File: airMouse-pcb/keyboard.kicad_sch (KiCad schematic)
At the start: 69 parts, among them SW1 TACT, SW10 TACT, SW11 TACT, SW12 TACT, SW13 TACT, SW14 TACT, SW15 TACT, SW16 TACT, SW17 TACT, SW18 TACT, SW19 TACT, SW2 TACT, SW20 TACT, SW21 TACT, SW22 TACT, SW23 TACT, SW24 TACT, SW25 TACT, SW26 TACT, SW27 TACT, SW28 TACT, SW29 TACT, SW3 TACT, SW30 TACT, SW31 TACT, SW32 TACT, SW33 TACT, SW34 TACT, SW35 TACT, SW36 TACT, SW37 TACT, SW38 TACT, SW39 TACT, SW4 TACT, SW40 TACT, SW41 TACT, SW42 TACT, SW43 TACT, SW44 TACT, SW45 TACT, SW46 TACT, SW47 TACT, SW48 TACT, SW49 TACT, SW5 TACT, SW6 TACT, SW7 TACT, SW8 TACT, SW9 TACT

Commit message: key footprint
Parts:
- SW1, SW10, SW11, SW12, SW13, SW14, SW15, SW16, SW17, SW18, SW19, SW2, SW20, SW21, SW22, SW23, SW24, SW25, SW26, SW27, SW28, SW29, SW3, SW30, SW31, SW32, SW33, SW34, SW35, SW36, SW37, SW38, SW39, SW4, SW40, SW41, SW42, SW43, SW44, SW45, SW46, SW47, SW48, SW49, SW5, SW6, SW7, SW8, SW9: footprint (none) -> airMouseLib:TL3315NF100Q
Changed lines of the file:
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@@
 			)
 		)
-		(property "Footprint" ""
+		(property "Footprint" "airMouseLib:TL3315NF100Q"
 			(at 68.58 100.33 0)
 			(effects
@@
 			)
 		)
-		(property "Footprint" ""
+		(property "Footprint" "airMouseLib:TL3315NF100Q"
 			(at 132.08 115.57 0)
 			(effects
@@
 			)
 		)
-		(property "Footprint" ""
+		(property "Footprint" "airMouseLib:TL3315NF100Q"
 			(at 106.68 100.33 0)
 			(effects
@@
 			)
 		)
-		(property "Footprint" ""
+		(property "Footprint" "airMouseLib:TL3315NF100Q"
 			(at 132.08 100.33 0)
 			(effects
@@
 			)
 		)
-		(property "Footprint" ""
+		(property "Footprint" "airMouseLib:TL3315NF100Q"
 			(at 170.18 85.09 0)
 			(effects
@@
 			)
 		)
-		(property "Footprint" ""
+		(property "Footprint" "airMouseLib:TL3315NF100Q"
 			(at 170.18 69.85 0)
 			(effects
@@
 			)
 		)
-		(property "Footprint" ""
+		(property "Footprint" "airMouseLib:TL3315NF100Q"
 			(at 144.78 100.33 0)
 			(effects
@@
 			)
 		)
-		(property "Footprint" ""
+		(property "Footprint" "airMouseLib:TL3315NF100Q"
 			(at 157.48 115.57 0)
 			(effects
@@
 			)
 		)
-		(property "Footprint" ""
+		(property "Footprint" "airMouseLib:TL3315NF100Q"
 			(at 182.88 130.81 0)
 			(effects
@@
 			)
 		)
-		(property "Footprint" ""
+		(property "Footprint" "airMouseLib:TL3315NF100Q"
 			(at 144.78 85.09 0)
 			(effects
@@
 			)
 		)
-		(property "Footprint" ""
+		(property "Footprint" "airMouseLib:TL3315NF100Q"
 			(at 157.48 85.09 0)
 			(effects
@@
 			)
 		)
-		(property "Footprint" ""
+		(property "Footprint" "airMouseLib:TL3315NF100Q"
 			(at 93.98 100.33 0)
 			(effects
@@
 			)
 		)
-		(property "Footprint" ""
+		(property "Footprint" "airMouseLib:TL3315NF100Q"
 			(at 125.73 130.81 0)
 			(effects
@@
 			)
 		)
-		(property "Footprint" ""
+		(property "Footprint" "airMouseLib:TL3315NF100Q"
 			(at 170.18 130.81 0)
 			(effects
@@
 			)
 		)
-		(property "Footprint" ""
+		(property "Footprint" "airMouseLib:TL3315NF100Q"
 			(at 170.18 115.57 0)
 			(effects
@@
 			)
 		)
-		(property "Footprint" ""
+		(property "Footprint" "airMouseLib:TL3315NF100Q"
 			(at 170.18 100.33 0)
 			(effects
@@
 			)
 		)
-		(property "Footprint" ""
+		(property "Footprint" "airMouseLib:TL3315NF100Q"
 			(at 119.38 85.09 0)
 			(effects
@@
 			)
 		)
-		(property "Footprint" ""
+		(property "Footprint" "airMouseLib:TL3315NF100Q"
 			(at 182.88 115.57 0)
 			(effects
@@
 			)
 		)
-		(property "Footprint" ""
+		(property "Footprint" "airMouseLib:TL3315NF100Q"
 			(at 68.58 115.57 0)
 			(effects
@@
 			)
 		)
-		(property "Footprint" ""
+		(property "Footprint" "airMouseLib:TL3315NF100Q"
 			(at 119.38 115.57 0)
 			(effects
@@
 			)
 		)
-		(property "Footprint" ""
+		(property "Footprint" "airMouseLib:TL3315NF100Q"
 			(at 81.28 69.85 0)
 			(effects
@@
 			)
 		)
-		(property "Footprint" ""
+		(property "Footprint" "airMouseLib:TL3315NF100Q"
 			(at 81.28 100.33 0)
 			(effects
@@
 			)
 		)
-		(property "Footprint" ""
+		(property "Footprint" "airMouseLib:TL3315NF100Q"
 			(at 182.88 85.09 0)
 			(effects
@@
 			)
 		)
-		(property "Footprint" ""
+		(property "Footprint" "airMouseLib:TL3315NF100Q"
 			(at 81.28 115.57 0)
 			(effects
@@
 			)
 		)
-		(property "Footprint" ""
+		(property "Footprint" "airMouseLib:TL3315NF100Q"
 			(at 144.78 115.57 0)
 			(effects
@@
 			)
 		)
-		(property "Footprint" ""
+		(property "Footprint" "airMouseLib:TL3315NF100Q"
 			(at 119.38 100.33 0)
 			(effects
@@
 			)
 		)
-		(property "Footprint" ""
+		(property "Footprint" "airMouseLib:TL3315NF100Q"
 			(at 182.88 69.85 0)
 			(effects
@@
 			)
 		)
-		(property "Footprint" ""
+		(property "Footprint" "airMouseLib:TL3315NF100Q"
 			(at 106.68 115.57 0)
 			(effects
@@
 			)
 		)
-		(property "Footprint" ""
+		(property "Footprint" "airMouseLib:TL3315NF100Q"
 			(at 119.38 69.85 0)
 			(effects
@@
 			)
 		)
-		(property "Footprint" ""
+		(property "Footprint" "airMouseLib:TL3315NF100Q"
 			(at 132.08 69.85 0)
 			(effects
@@
 			)
 		)
-		(property "Footprint" ""
+		(property "Footprint" "airMouseLib:TL3315NF100Q"
 			(at 157.48 100.33 0)
 			(effects
@@
 			)
 		)
-		(property "Footprint" ""
+		(property "Footprint" "airMouseLib:TL3315NF100Q"
 			(at 68.58 130.81 0)
 			(effects
@@
 			)
 		)
-		(property "Footprint" ""
+		(property "Footprint" "airMouseLib:TL3315NF100Q"
 			(at 81.28 130.81 0)
 			(effects
@@
 			)
 		)
-		(property "Footprint" ""
+		(property "Footprint" "airMouseLib:TL3315NF100Q"
 			(at 93.98 130.81 0)
 			(effects
@@
 			)
 		)
-		(property "Footprint" ""
+		(property "Footprint" "airMouseLib:TL3315NF100Q"
 			(at 93.98 85.09 0)
 			(effects
@@
 			)
 		)
-		(property "Footprint" ""
+		(property "Footprint" "airMouseLib:TL3315NF100Q"
 			(at 157.48 130.81 0)
 			(effects
@@
 			)
 		)
-		(property "Footprint" ""
+		(property "Footprint" "airMouseLib:TL3315NF100Q"
 			(at 81.28 85.09 0)
 			(effects
@@
 			)
 		)
-		(property "Footprint" ""
+		(property "Footprint" "airMouseLib:TL3315NF100Q"
 			(at 182.88 100.33 0)
 			(effects
@@
 			)
 		)
-		(property "Footprint" ""
+		(property "Footprint" "airMouseLib:TL3315NF100Q"
 			(at 144.78 69.85 0)
 			(effects
@@
 			)
 		)
-		(property "Footprint" ""
+		(property "Footprint" "airMouseLib:TL3315NF100Q"
 			(at 157.48 69.85 0)
 			(effects
@@
 			)
 		)
-		(property "Footprint" ""
+		(property "Footprint" "airMouseLib:TL3315NF100Q"
 			(at 93.98 69.85 0)
 			(effects
@@
 			)
 		)
-		(property "Footprint" ""
+		(property "Footprint" "airMouseLib:TL3315NF100Q"
 			(at 93.98 115.57 0)
 			(effects
@@
 			)
 		)
-		(property "Footprint" ""
+		(property "Footprint" "airMouseLib:TL3315NF100Q"
 			(at 68.58 69.85 0)
 			(effects
@@
 			)
 		)
-		(property "Footprint" ""
+		(property "Footprint" "airMouseLib:TL3315NF100Q"
 			(at 132.08 85.09 0)
 			(effects
@@
 			)
 		)
-		(property "Footprint" ""
+		(property "Footprint" "airMouseLib:TL3315NF100Q"
 			(at 106.68 130.81 0)
 			(effects
@@
 			)
 		)
-		(property "Footprint" ""
+		(property "Footprint" "airMouseLib:TL3315NF100Q"
 			(at 68.58 85.09 0)
 			(effects
@@
 			)
 		)
-		(property "Footprint" ""
+		(property "Footprint" "airMouseLib:TL3315NF100Q"
 			(at 144.78 130.81 0)
 			(effects
@@
 			)
 		)
-		(property "Footprint" ""
+		(property "Footprint" "airMouseLib:TL3315NF100Q"
 			(at 106.68 85.09 0)
 			(effects
@@
 			)
 		)
-		(property "Footprint" ""
+		(property "Footprint" "airMouseLib:TL3315NF100Q"
 			(at 106.68 69.85 0)
 			(effects

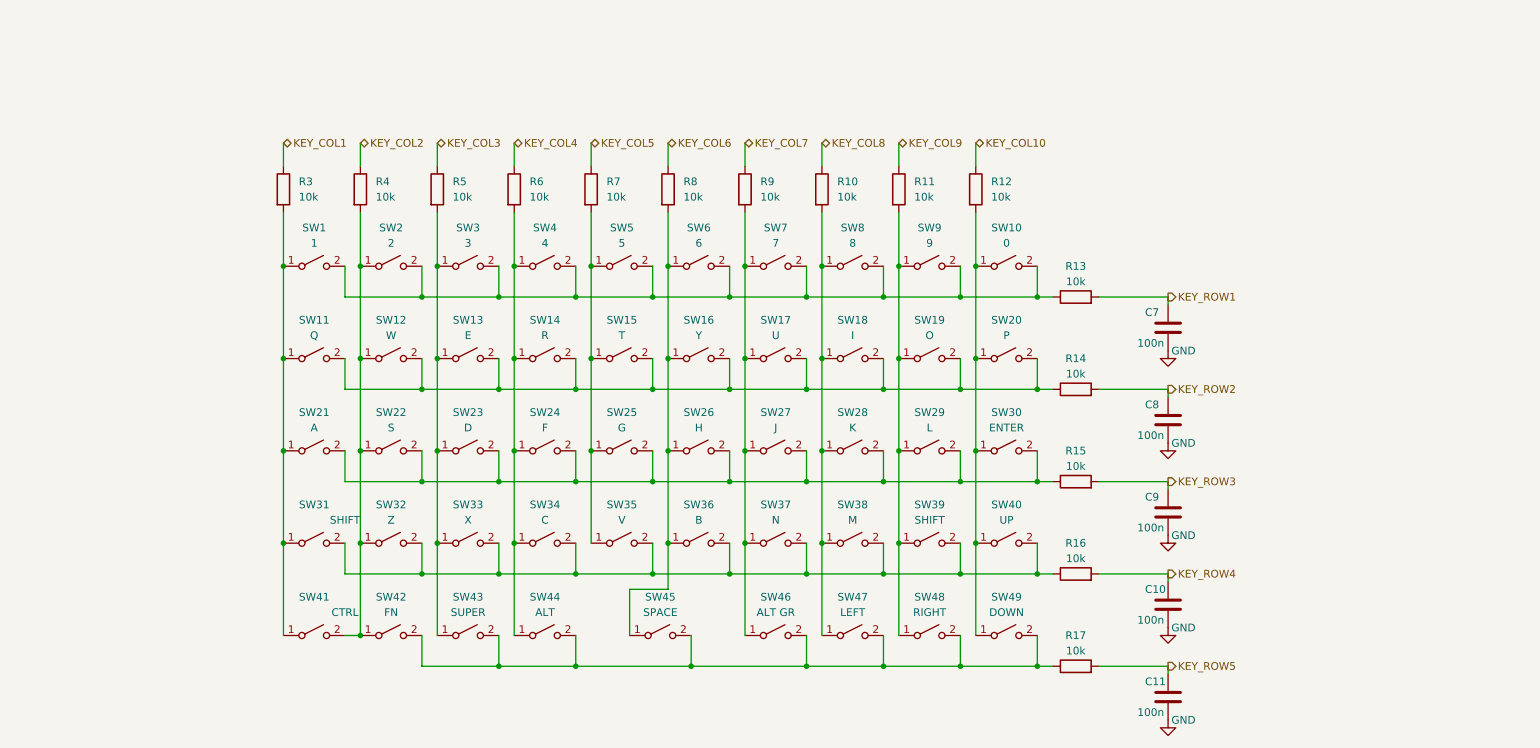
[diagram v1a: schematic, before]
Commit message: add keyboard
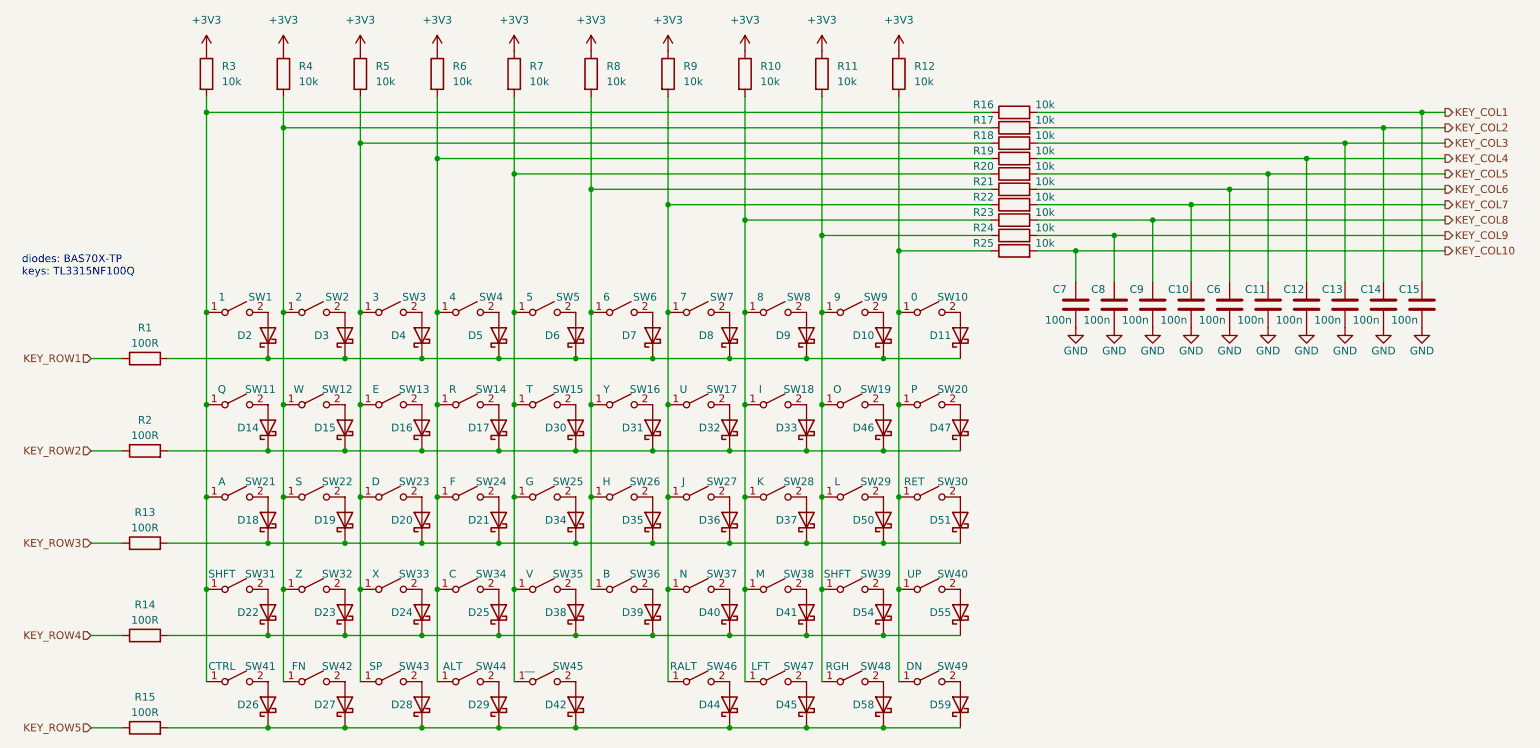
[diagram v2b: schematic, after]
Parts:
- removed SW1, SW10, SW11, SW12, SW13, SW14, SW15, SW16, SW17, SW18, SW19, SW2, SW20, SW21, SW22, SW23, SW24, SW25, SW26, SW27, SW28, SW29, SW3, SW30, SW31, SW32, SW33, SW34, SW35, SW36, SW37, SW38, SW39, SW4, SW40, SW41, SW42, SW43, SW44, SW45, SW46, SW47, SW48, SW49, SW5, SW6, SW7, SW8, SW9: TACT, airMouseLib:TL3315NF100Q, symbol Switch:SW_SPST
- added C12, C13, C14, C15, C6: 100n, Capacitor_SMD:C_0603_1608Metric, symbol Device:C
- added D10, D11, D14, D15, D16, D17, D18, D19, D2, D20, D21, D22, D23, D24, D25, D26, D27, D28, D29, D3, D30, D31, D32, D33, D34, D35, D36, D37, D38, D39, D4, D40, D41, D42, D44, D45, D46, D47, D5, D50, D51, D54, D55, D58, D59, D6, D7, D8, D9: BAS70X-TP, Diode_SMD:D_SOD-523, symbol Device:D_Schottky
- added R1, R2: 100R, Resistor_SMD:R_0603_1608Metric, symbol Device:R
- added R18, R19, R20, R21, R22, R23, R24, R25: 10k, Resistor_SMD:R_0603_1608Metric, symbol Device:R
- added SW1, SW10, SW11, SW12, SW13, SW14, SW15, SW16, SW17, SW18, SW19, SW2, SW20, SW21, SW22, SW23, SW24, SW25, SW26, SW27, SW28, SW29, SW3, SW30, SW31, SW32, SW33, SW34, SW35, SW36, SW37, SW38, SW39, SW4, SW40, SW41, SW42, SW43, SW44, SW45, SW46, SW47, SW48, SW49, SW5, SW6, SW7, SW8, SW9: KEY, airMouseLib:TL3315NF100Q, symbol airMouseLib:KEY
- C10, C11, C7, C8, C9: footprint (none) -> Capacitor_SMD:C_0603_1608Metric
- R10, R11, R12, R16, R17, R3, R4, R5, R6, R7, R8, R9: footprint (none) -> Resistor_SMD:R_0603_1608Metric
- R13, R14, R15: value 10k -> 100R; footprint (none) -> Resistor_SMD:R_0603_1608Metric
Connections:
- net GND: now also C12.2, C13.2, C14.2, C15.2, C6.2
- net KEY_COL1: now also R16.2, C15.1; no longer R3.1
- net KEY_COL10: now also C7.1, R25.2; no longer R12.1
- net KEY_COL2: now also R17.2, C14.1; no longer R4.1
- net KEY_COL3: now also C13.1, R18.2; no longer R5.1
- net KEY_COL4: now also C12.1, R19.2; no longer R6.1
- net KEY_COL5: now also C11.1, R20.2; no longer R7.1
- net KEY_COL6: now also C6.1, R21.2; no longer R8.1
- net KEY_COL7: now also C10.1, R22.2; no longer R9.1
- net KEY_COL8: now also C9.1, R23.2; no longer R10.1
- net KEY_COL9: now also C8.1, R24.2; no longer R11.1
- net KEY_ROW1: now also R1.1; no longer C7.1, R13.2
- net KEY_ROW2: now also R2.1; no longer C8.1, R14.2
- net KEY_ROW3: now also R13.1; no longer C9.1, R15.2
- net KEY_ROW4: now also R14.1; no longer C10.1, R16.2
- net KEY_ROW5: now also R15.1; no longer C11.1, R17.2
- net at R3.2: now also R16.1, SW1.1 (A), SW11.1 (A), SW21.1 (A), SW31.1 (A), SW41.1 (A)
- net at R6.2: now also R19.1, SW14.1 (A), SW24.1 (A), SW34.1 (A), SW4.1 (A), SW44.1 (A)
- net at R8.2: now also R21.1, SW16.1 (A), SW26.1 (A), SW36.1 (A), SW6.1 (A)
- net at R11.2: now also R24.1, SW19.1 (A), SW29.1 (A), SW39.1 (A), SW48.1 (A), SW9.1 (A)
- net at R9.2: now also R22.1, SW17.1 (A), SW27.1 (A), SW37.1 (A), SW46.1 (A), SW7.1 (A)
- net at R10.2: now also R23.1, SW18.1 (A), SW28.1 (A), SW38.1 (A), SW47.1 (A), SW8.1 (A)
- net at R12.2: now also R25.1, SW10.1 (A), SW20.1 (A), SW30.1 (A), SW40.1 (A), SW49.1 (A)
- net at R17.1: now also R4.2, SW12.1 (A), SW2.1 (A), SW22.1 (A), SW32.1 (A), SW42.1 (A)
- net at R5.2: now also R18.1, SW13.1 (A), SW23.1 (A), SW3.1 (A), SW33.1 (A), SW43.1 (A)
- net at R7.2: now also R20.1, SW15.1 (A), SW25.1 (A), SW35.1 (A), SW45.1 (A), SW5.1 (A)
- new net: D9.2 (A), SW8.2 (B)
- new net: D40.2 (A), SW37.2 (B)
- new net: D26.1 (K), D27.1 (K), D28.1 (K), D29.1 (K), D42.1 (K), D44.1 (K), D45.1 (K), D58.1 (K), D59.1 (K), R15.2
- new net: D26.2 (A), SW41.2 (B)
- new net: D32.2 (A), SW17.2 (B)
- new net: D10.1 (K), D11.1 (K), D2.1 (K), D3.1 (K), D4.1 (K), D5.1 (K), D6.1 (K), D7.1 (K), D8.1 (K), D9.1 (K), R1.2
- new net: D3.2 (A), SW2.2 (B)
- new net: D14.1 (K), D15.1 (K), D16.1 (K), D17.1 (K), D30.1 (K), D31.1 (K), D32.1 (K), D33.1 (K), D46.1 (K), D47.1 (K), R2.2
- new net: D30.2 (A), SW15.2 (B)
- new net: D42.2 (A), SW45.2 (B)
- new net: D18.1 (K), D19.1 (K), D20.1 (K), D21.1 (K), D34.1 (K), D35.1 (K), D36.1 (K), D37.1 (K), D50.1 (K), D51.1 (K), R13.2
- new net: D36.2 (A), SW27.2 (B)
- new net: D23.2 (A), SW32.2 (B)
- new net: D19.2 (A), SW22.2 (B)
- new net: D22.1 (K), D23.1 (K), D24.1 (K), D25.1 (K), D38.1 (K), D39.1 (K), D40.1 (K), D41.1 (K), D54.1 (K), D55.1 (K), R14.2
- new net: D47.2 (A), SW20.2 (B)
- new net: D33.2 (A), SW18.2 (B)
- new net: D31.2 (A), SW16.2 (B)
- new net: D17.2 (A), SW14.2 (B)
- new net: D24.2 (A), SW33.2 (B)
- new net: D28.2 (A), SW43.2 (B)
- new net: D44.2 (A), SW46.2 (B)
- new net: D14.2 (A), SW11.2 (B)
- new net: D15.2 (A), SW12.2 (B)
- new net: D46.2 (A), SW19.2 (B)
- new net: D45.2 (A), SW47.2 (B)
- new net: D50.2 (A), SW29.2 (B)
- new net: D41.2 (A), SW38.2 (B)
- new net: D8.2 (A), SW7.2 (B)
- new net: D27.2 (A), SW42.2 (B)
- new net: D37.2 (A), SW28.2 (B)
- new net: D22.2 (A), SW31.2 (B)
- new net: D6.2 (A), SW5.2 (B)
- new net: D54.2 (A), SW39.2 (B)
- new net: D20.2 (A), SW23.2 (B)
- new net: D35.2 (A), SW26.2 (B)
- new net: D39.2 (A), SW36.2 (B)
- new net: D4.2 (A), SW3.2 (B)
- new net: D11.2 (A), SW10.2 (B)
- new net: D25.2 (A), SW34.2 (B)
- new net: D55.2 (A), SW40.2 (B)
- new net: D21.2 (A), SW24.2 (B)
- new net: D34.2 (A), SW25.2 (B)
- new net: D58.2 (A), SW48.2 (B)
- new net: D16.2 (A), SW13.2 (B)
- new net: D51.2 (A), SW30.2 (B)
- new net: D5.2 (A), SW4.2 (B)
- new net: D7.2 (A), SW6.2 (B)
- new net: D2.2 (A), SW1.2 (B)
- new net: D38.2 (A), SW35.2 (B)
- new net: D10.2 (A), SW9.2 (B)
- new net: D18.2 (A), SW21.2 (B)
- new net: D29.2 (A), SW44.2 (B)
- new net: D59.2 (A), SW49.2 (B)
- new net +3V3: R10.1, R11.1, R12.1, R3.1, R4.1, R5.1, R6.1, R7.1, R8.1, R9.1
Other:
- note added: "diodes: BAS70X-TP keys: TL3315NF100Q"
- moved on the sheet: C10, C7, C8, C9, R10, R11, R12, R3, R4, R5, R6, R7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

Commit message: page data
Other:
- company: (none) -> Bart's Design
- title: (none) -> EtherPointer
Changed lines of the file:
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@@
 	(generator_version "8.0")
 	(paper "A4")
+	(title_block
+		(title "EtherPointer")
+		(date "2025-02-13")
+		(rev "RC1")
+		(company "Bart's Design")
+		(comment 1 "Bartosz Pracz")
+	)
 	(junction
 		(at 86.36 100.33)
